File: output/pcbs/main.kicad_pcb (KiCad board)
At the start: 2 copper layers, 228.1 x 75.7 mm, 140 parts

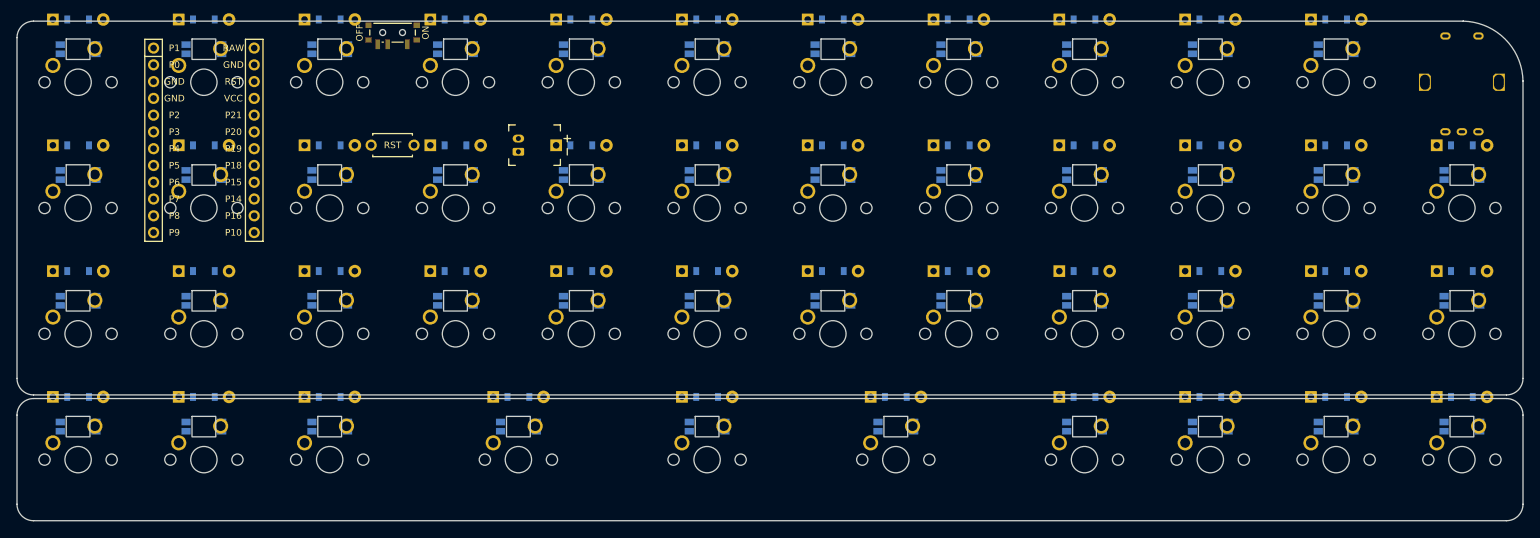
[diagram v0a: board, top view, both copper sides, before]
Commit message: Fix outline gap between matrix and modrow zones
- Add expand: 0.5 to bounds outline to merge matrix and modrow zones
- Eliminates the 0.5mm gap that required manual KiCad fix
- Single continuous outline, no internal edges
- Margins: 9.75mm (9.25 keycap + 0.5 expand)
- 2.5mm rounded corners preserved
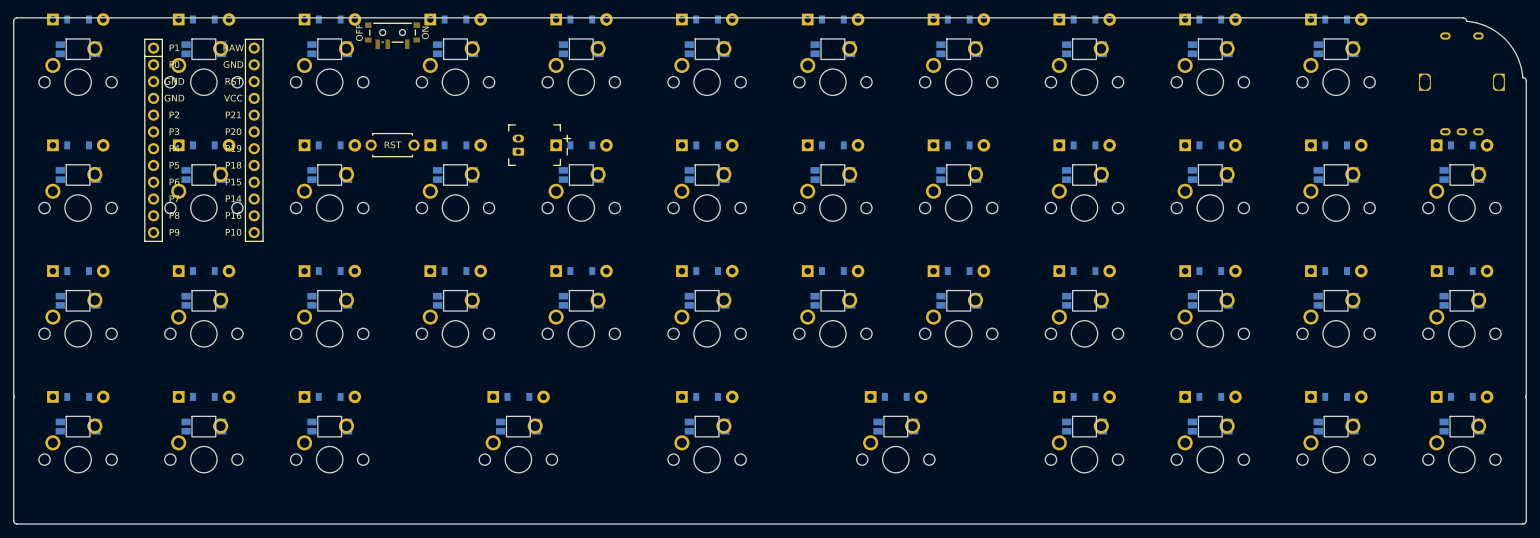
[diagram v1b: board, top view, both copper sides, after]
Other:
- board size 228.1 x 75.7 mm -> 229.1 x 76.7 mm
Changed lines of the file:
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@@
   (title_block
     (title "main")
-    (date "2026-07-12")
+    (date "2026-07-13")
     (rev "v1.0.0")
     (company "Unknown")
@@
         (pad "2" thru_hole oval (at 1 0 90) (size 1.2 1.75) (drill 0.75) (layers "*.Cu" "*.Mask") (net 143 "BAT_P"))
     )
-  (gr_line (start 43.25 33.6) (end 259.75 33.60000000000001) (layer Edge.Cuts) (stroke (width 0.15) (type default)))
-(gr_line (start 40.75 87.7) (end 40.75 36.1) (layer Edge.Cuts) (stroke (width 0.15) (type default)))
-(gr_line (start 43.25 90.2) (end 266.3 90.2) (layer Edge.Cuts) (stroke (width 0.15) (type default)))
-(gr_line (start 259.75 33.6) (end 259.75 33.60216240000001) (layer Edge.Cuts) (stroke (width 0.15) (type default)))
-(gr_line (start 268.8 87.7) (end 268.8 42.650000000000006) (layer Edge.Cuts) (stroke (width 0.15) (type default)))
-(gr_line (start 268.79783760000004 42.650000000000006) (end 268.8 42.650000000000006) (layer Edge.Cuts) (stroke (width 0.15) (type default)))
-(gr_line (start 43.25 109.25) (end 266.3 109.25) (layer Edge.Cuts) (stroke (width 0.15) (type default)))
-(gr_line (start 43.25 90.75) (end 266.3 90.75) (layer Edge.Cuts) (stroke (width 0.15) (type default)))
-(gr_line (start 40.75 93.25) (end 40.75 106.75) (layer Edge.Cuts) (stroke (width 0.15) (type default)))
-(gr_line (start 268.8 106.75) (end 268.8 93.25) (layer Edge.Cuts) (stroke (width 0.15) (type default)))
-(gr_arc (start 268.79783760000004 42.650000000000006) (mid 266.09073770000003 36.30926230000001) (end 259.75 33.60216240000001) (layer Edge.Cuts) (stroke (width 0.15) (type default)))
-(gr_arc (start 266.3 90.2) (mid 268.067767 89.46776700000001) (end 268.8 87.7) (layer Edge.Cuts) (stroke (width 0.15) (type default)))
-(gr_arc (start 40.75 87.7) (mid 41.482233 89.46776700000001) (end 43.25 90.2) (layer Edge.Cuts) (stroke (width 0.15) (type default)))
-(gr_arc (start 43.25 33.6) (mid 41.482233 34.332233) (end 40.75 36.1) (layer Edge.Cuts) (stroke (width 0.15) (type default)))
-(gr_arc (start 266.3 109.25) (mid 268.067767 108.517767) (end 268.8 106.75) (layer Edge.Cuts) (stroke (width 0.15) (type default)))
-(gr_arc (start 268.8 93.25) (mid 268.067767 91.482233) (end 266.3 90.75) (layer Edge.Cuts) (stroke (width 0.15) (type default)))
-(gr_arc (start 43.25 90.75) (mid 41.482233 91.482233) (end 40.75 93.25) (layer Edge.Cuts) (stroke (width 0.15) (type default)))
-(gr_arc (start 40.75 106.75) (mid 41.482233 108.517767) (end 43.25 109.25) (layer Edge.Cuts) (stroke (width 0.15) (type default)))
+  (gr_line (start 40.75 33.1) (end 259.75 33.1) (layer Edge.Cuts) (stroke (width 0.15) (type default)))
+(gr_arc (start 260.25 33.6) (mid 260.1035534 33.2464466) (end 259.75 33.1) (layer Edge.Cuts) (stroke (width 0.15) (type default)))
+(gr_line (start 260.25 33.6) (end 260.25 33.62652450000001) (layer Edge.Cuts) (stroke (width 0.15) (type default)))
+(gr_line (start 268.7734755 42.150000000000006) (end 268.8 42.150000000000006) (layer Edge.Cuts) (stroke (width 0.15) (type default)))
+(gr_arc (start 269.3 42.650000000000006) (mid 269.1535534 42.2964466) (end 268.8 42.150000000000006) (layer Edge.Cuts) (stroke (width 0.15) (type default)))
+(gr_line (start 269.3 90.2) (end 269.3 42.650000000000006) (layer Edge.Cuts) (stroke (width 0.15) (type default)))
+(gr_arc (start 269.2175823 90.47500000000001) (mid 269.2789526 90.3435424) (end 269.3 90.2) (layer Edge.Cuts) (stroke (width 0.15) (type default)))
+(gr_arc (start 269.3 90.75) (mid 269.2789526 90.6064576) (end 269.2175823 90.475) (layer Edge.Cuts) (stroke (width 0.15) (type default)))
+(gr_line (start 269.3 109.25) (end 269.3 90.75) (layer Edge.Cuts) (stroke (width 0.15) (type default)))
+(gr_arc (start 268.8 109.75) (mid 269.1535534 109.6035534) (end 269.3 109.25) (layer Edge.Cuts) (stroke (width 0.15) (type default)))
+(gr_line (start 40.75 109.75) (end 268.8 109.75) (layer Edge.Cuts) (stroke (width 0.15) (type default)))
+(gr_arc (start 40.25 109.25) (mid 40.3964466 109.6035534) (end 40.75 109.75) (layer Edge.Cuts) (stroke (width 0.15) (type default)))
+(gr_line (start 40.25 90.75) (end 40.25 109.25) (layer Edge.Cuts) (stroke (width 0.15) (type default)))
+(gr_arc (start 40.3324177 90.475) (mid 40.2710474 90.6064576) (end 40.25 90.75) (layer Edge.Cuts) (stroke (width 0.15) (type default)))
+(gr_arc (start 40.25 90.2) (mid 40.2710474 90.3435424) (end 40.3324177 90.47500000000001) (layer Edge.Cuts) (stroke (width 0.15) (type default)))
+(gr_line (start 40.25 90.2) (end 40.25 33.6) (layer Edge.Cuts) (stroke (width 0.15) (type default)))
+(gr_arc (start 40.75 33.1) (mid 40.3964466 33.2464466) (end 40.25 33.6) (layer Edge.Cuts) (stroke (width 0.15) (type default)))
+(gr_arc (start 268.7734755 42.150000000000006) (mid 266.09073770000003 36.30926230000001) (end 260.25 33.62652450000001) (layer Edge.Cuts) (stroke (width 0.15) (type default)))
 )

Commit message: Final outline: 228x76mm, 9.25mm margins, 2.5mm rounded corners
- Key bounds 17.5mm + expand 0.5mm = 9.25mm uniform margins
- 2.5mm fillet on all corners
- Knob circle at top-right (9.25mm radius)
- Note: 0.5mm gap between matrix/modrow zones (ergogen limitation)
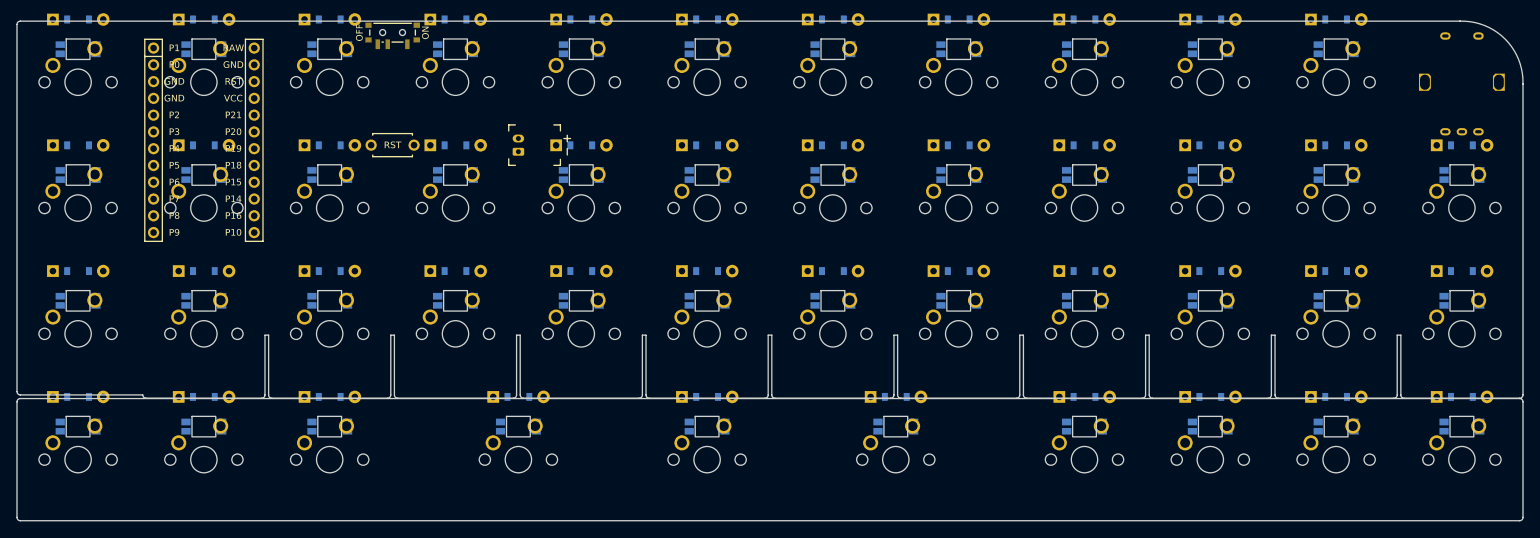
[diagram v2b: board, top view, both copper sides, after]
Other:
- board size 229.1 x 76.7 mm -> 228.1 x 75.7 mm
